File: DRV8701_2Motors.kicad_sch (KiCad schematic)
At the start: 37 parts, among them J1 Conn_01x02, J2 Conn_01x10, J3 Conn_01x10, SW1 SW_SPDT_321, U3 AM26LV32xD, U4 AM26LV32xD

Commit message: modif footprints des condo de puissance
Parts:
- C1, C3, C4: footprint Capacitor_SMD:C_0402_1005Metric -> Capacitor_SMD:C_0603_1608Metric
- C2: footprint Capacitor_SMD:C_0402_1005Metric -> Capacitor_SMD:C_1206_3216Metric
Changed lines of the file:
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@@
 			)
 		)
-		(property "Footprint" "Capacitor_SMD:C_0402_1005Metric"
+		(property "Footprint" "Capacitor_SMD:C_0603_1608Metric"
 			(at 59.3852 124.46 0)
 			(effects
@@
 			)
 		)
-		(property "Footprint" "Capacitor_SMD:C_0402_1005Metric"
+		(property "Footprint" "Capacitor_SMD:C_0603_1608Metric"
 			(at 56.8452 91.44 0)
 			(effects
@@
 			)
 		)
-		(property "Footprint" "Capacitor_SMD:C_0402_1005Metric"
+		(property "Footprint" "Capacitor_SMD:C_0603_1608Metric"
 			(at 25.0952 91.44 0)
 			(effects
@@
 			)
 		)
-		(property "Footprint" "Capacitor_SMD:C_0402_1005Metric"
+		(property "Footprint" "Capacitor_SMD:C_1206_3216Metric"
 			(at 35.2552 124.46 0)
 			(effects

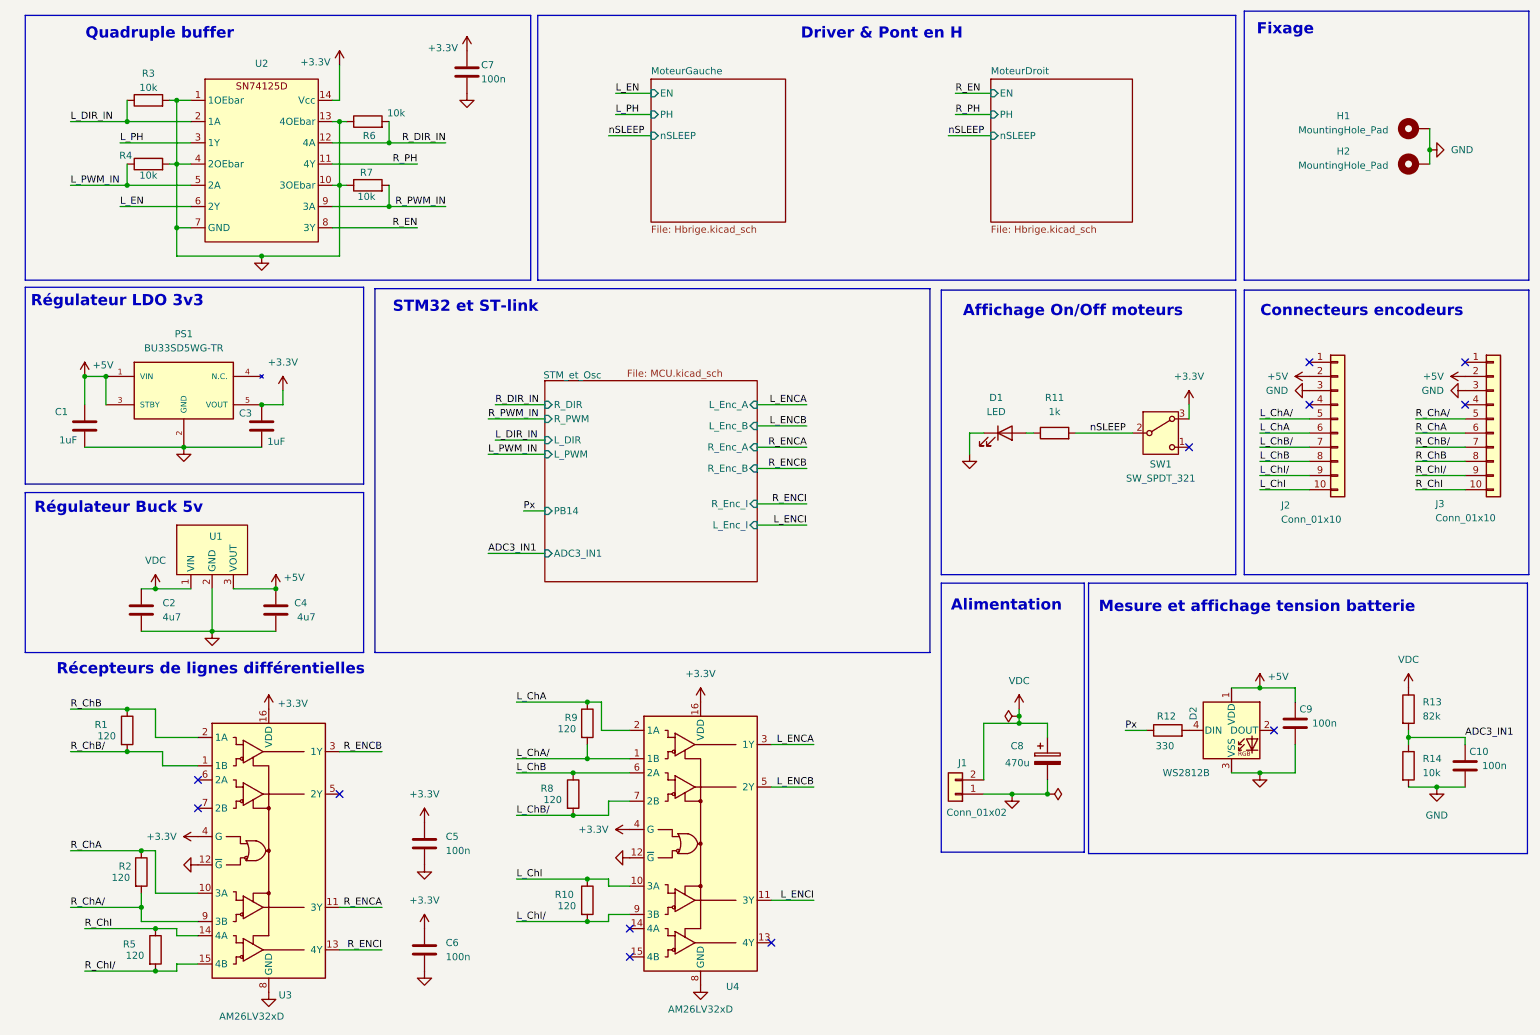
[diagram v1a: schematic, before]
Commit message: V2 Driver-- avec control de courant
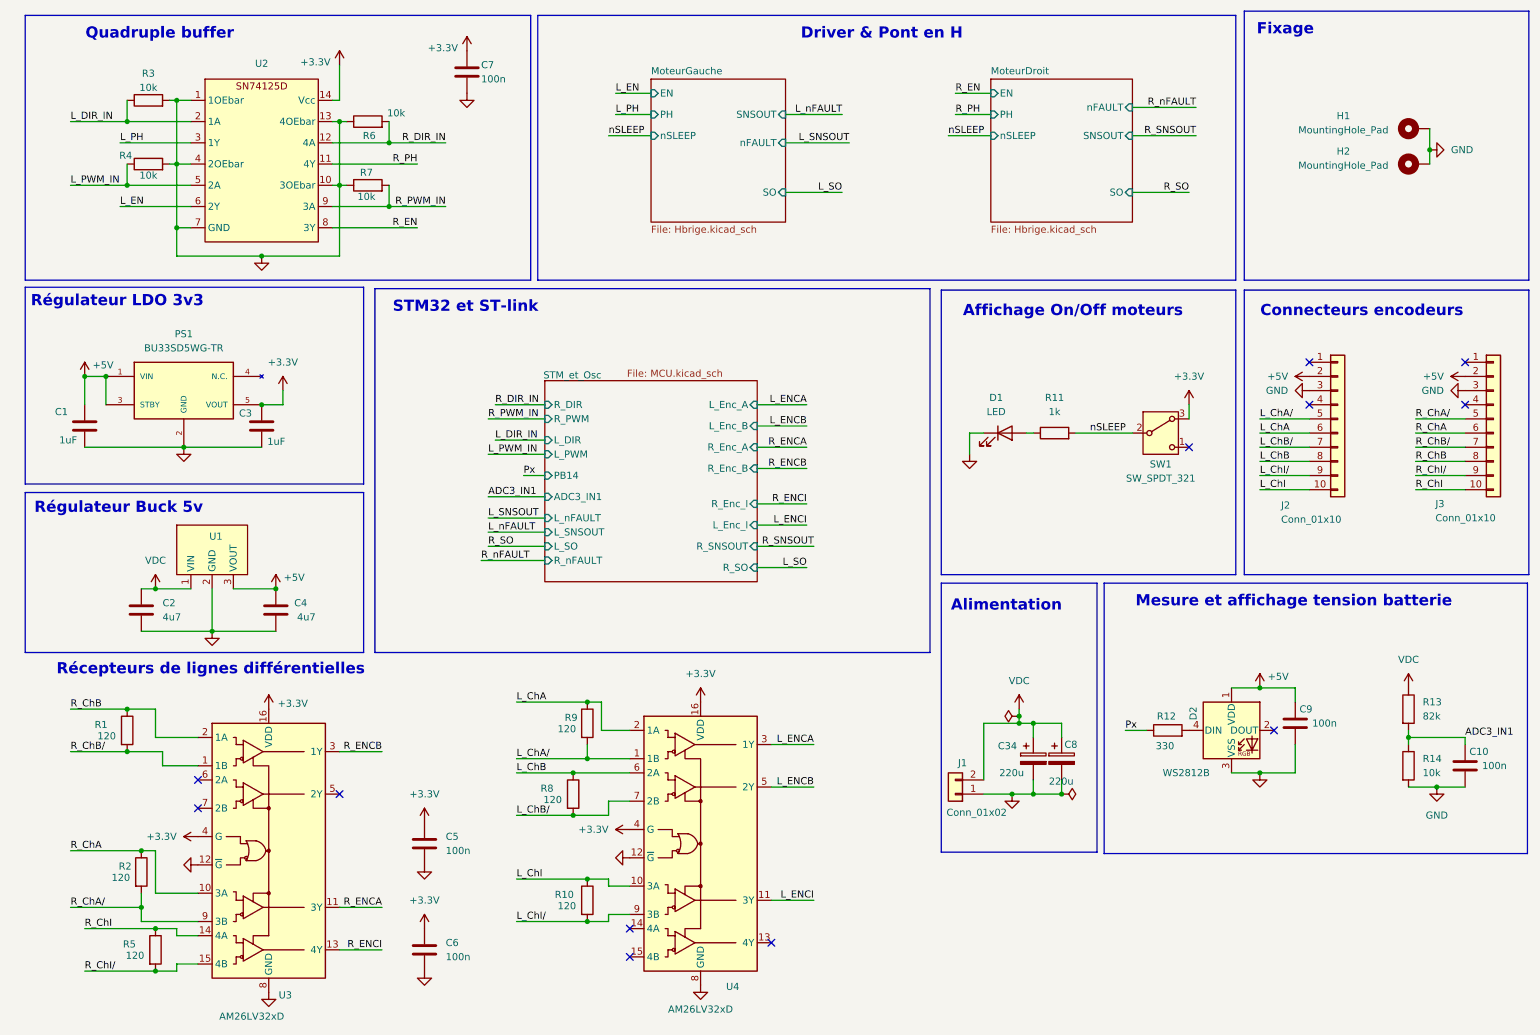
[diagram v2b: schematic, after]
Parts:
- added C34: 220u, ECA1HHG471:ECA1HHG471, symbol Device:C_Polarized
- C8: value 470u -> 220u; footprint Capacitor:Wurth-470u-50V -> ECA1HHG471:ECA1HHG471; Field5 (none) -> EEU-FR1H221; MPN 860080678019 -> (none)
- R1, R10, R2, R5, R8, R9: footprint Resistor_SMD:R_0201_0603Metric -> Resistor_SMD:R_0402_1005Metric
- R11: footprint Resistor_SMD:R_0603_1608Metric -> Resistor_SMD:R_0402_1005Metric
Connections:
- net GND: now also C34.2
- net VDC: now also C34.1
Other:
- sheet MoteurDroit ports: added SNSOUT, SO, nFAULT; removed none
- sheet MoteurGauche ports: added SNSOUT, SO, nFAULT; removed none
- sheet STM_et_Osc ports: added L_SNSOUT, L_SO, L_nFAULT, R_SNSOUT, R_SO, R_nFAULT; removed none

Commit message: final push
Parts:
- removed SW1: SW_SPDT_321, switch:472121010111, symbol Switch:SW_SPDT_321
- U2: value ~ -> SN74HC125PWR
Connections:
- net nSLEEP: no longer R11.2
- new net LED_state: R11.2
- no-connect marks 12 -> 11
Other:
- sheet STM_et_Osc ports: added GPIO_PB10, GPIO_PB2; removed none
- note added: "LED de STATUT"
- note removed: "Affichage On/Off moteurs"
- moved on the sheet: D1, R11
